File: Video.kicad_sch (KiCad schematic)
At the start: 0 parts

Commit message: motherboard: Added SHIFTER to the schematic and tidied up a pile
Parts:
- added R102: 1k, rhais_rcl:R0603, symbol Device:R_Small
- added U13: 74LS04, symbol 74xx:74LS04
- added U15: 74LS86, symbol 74xx:74LS86
- added U40: GST_SHIFTER, Package_LCC:PLCC-84_SMD-Socket, symbol dragonSTe:GST_SHIFTER
- added U41: 74LS257, symbol 74xx:74LS257
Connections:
- new net: U13.3, U40.21 (SD7)
- new net: R102.1, U40.50 (MONO)
- new net: U41.2 (I0a), U41.6 (I1b)
- new net: U13.5, U15.3
- new net +5V: U40.11 (VDD), U40.32 (VDD), U41.16 (VCC), U41.5 (I0b)
- new net 32MHz: U41.3 (I1a)
- new net DE: U40.54 (DE)
- new net FCLK: U40.34 (FCLK)
- new net GND: U15.10, U15.4, U15.5, U15.9, U40.73 (LOWP), U40.74 (GND), U40.75 (GND), U41.10 (I1d), U41.11 (I0d), U41.13 (I1c), U41.14 (I0c), U41.15 (OE), U41.8 (GND)
- new net MC: U40.53 (CLK), U41.4 (Za)
- new net MICROWIRE_CLK: U40.31 (MWC)
- new net MICROWIRE_DATA: U40.30 (MWD)
- new net MONO_MON: U41.7 (Zb)
- new net SCLK: U40.33 (SCLK)
- new net Sound.D0: U40.28 (SD0)
- new net Sound.D1: U40.27 (SD1)
- new net Sound.D2: U40.26 (SD2)
- new net Sound.D3: U40.25 (SD3)
- new net Sound.D4: U40.24 (SD4)
- new net Sound.D5: U40.23 (SD5)
- new net Sound.D6: U40.22 (SD6)
- new net Sound.D7: U13.4
- new net SysBus.A1: U40.17 (A1)
- new net SysBus.A2: U40.16 (A2)
- new net SysBus.A3: U40.15 (A3)
- new net SysBus.A4: U40.14 (A4)
- new net SysBus.A5: U40.13 (A5)
- new net SysBus.A6: U40.12 (A6)
- new net SysBus.D0: U40.78 (PD0)
- new net SysBus.D1: U40.79 (PD1)
- new net SysBus.D10: U40.4 (PD10)
- new net SysBus.D11: U40.5 (PD11)
- new net SysBus.D12: U40.6 (PD12)
- new net SysBus.D13: U40.7 (PD13)
- new net SysBus.D14: U40.8 (PD14)
- new net SysBus.D15: U40.9 (PD15)
- new net SysBus.D2: U40.80 (PD2)
- new net SysBus.D3: U40.81 (PD3)
- new net SysBus.D4: U40.82 (PD4)
- new net SysBus.D5: U40.83 (PD5)
- new net SysBus.D6: U40.84 (PD6)
- new net SysBus.D7: U40.1 (PD7)
- new net SysBus.D8: U40.2 (PD8)
- new net SysBus.D9: U40.3 (PD9)
- new net SysBus.R/~{W}: U40.10 (R/~{W})
- new net ~{LD}: U40.19 (~{LD})
- new net ~{MICROWIRE_EN}: U40.29 (~{MWE})
- new net ~{RD}: U40.20 (~{RD})
- no-connect marks 0 -> 2

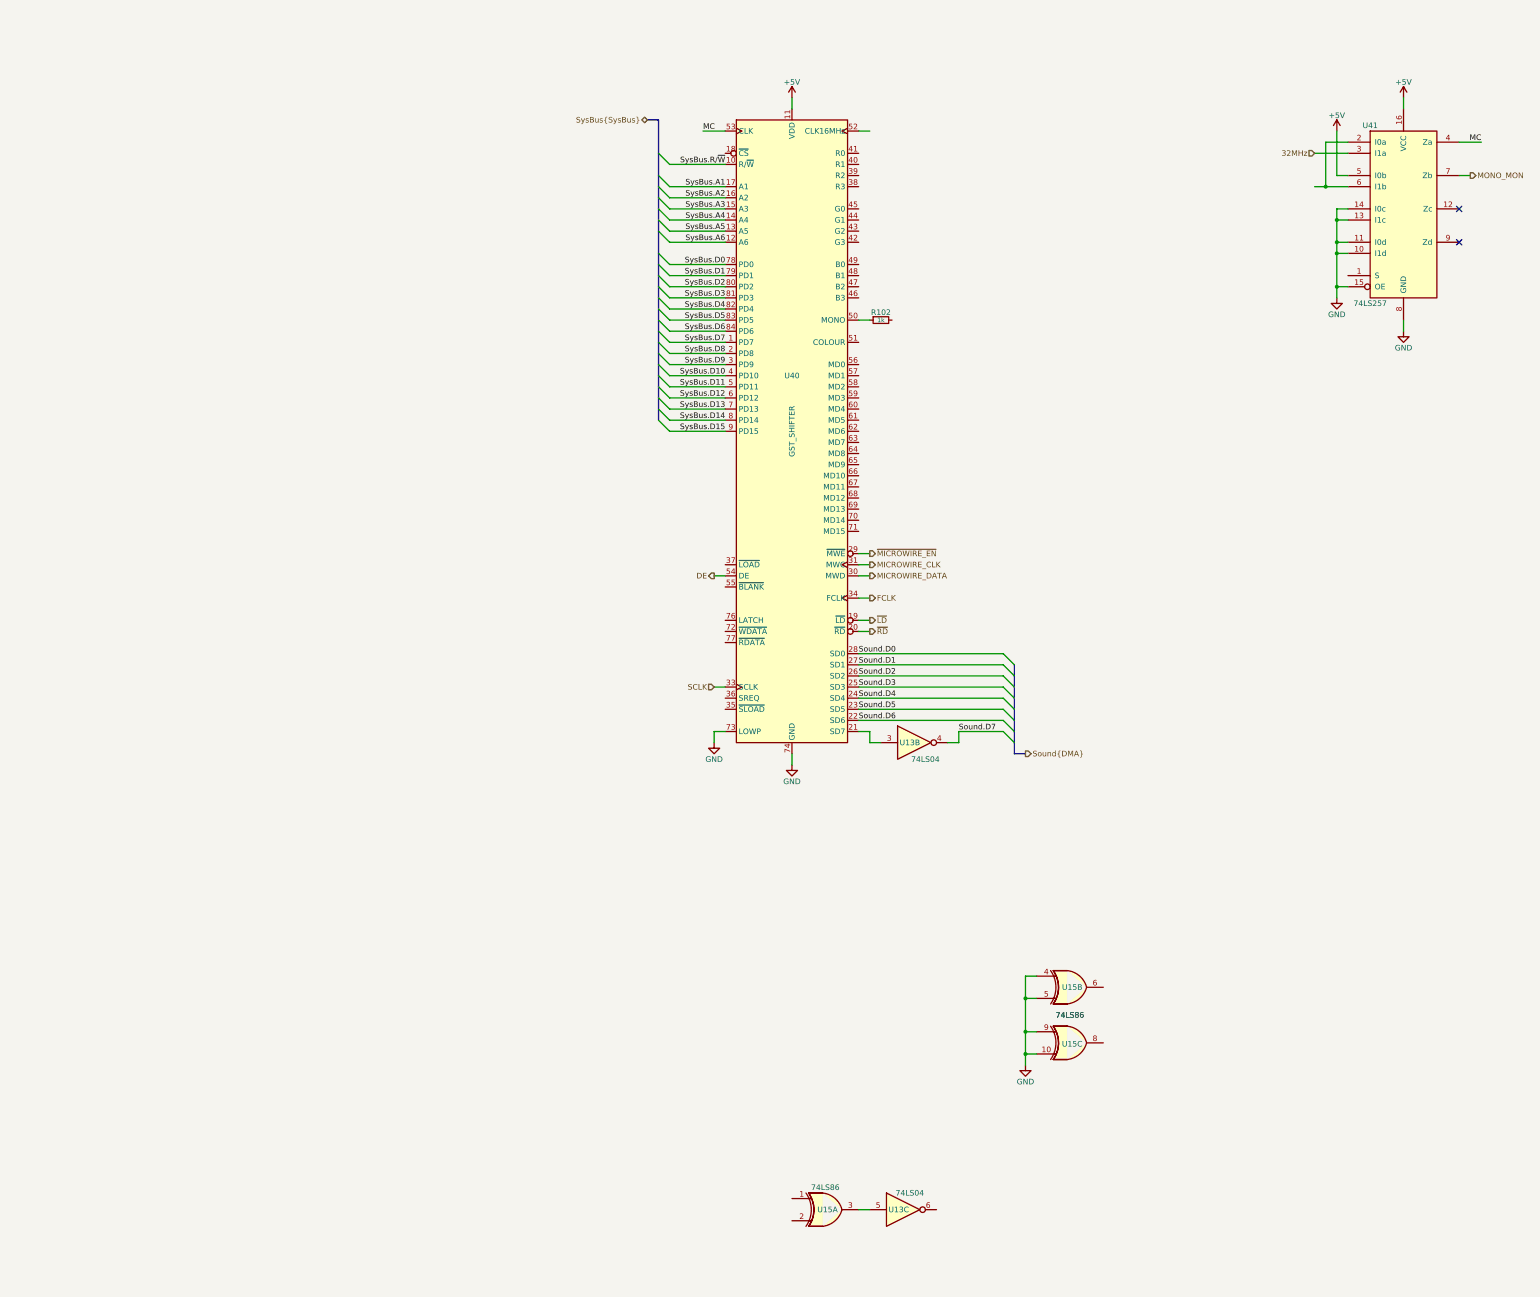
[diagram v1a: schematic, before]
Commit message: motherboard: Further filled out the schematic for the video interface
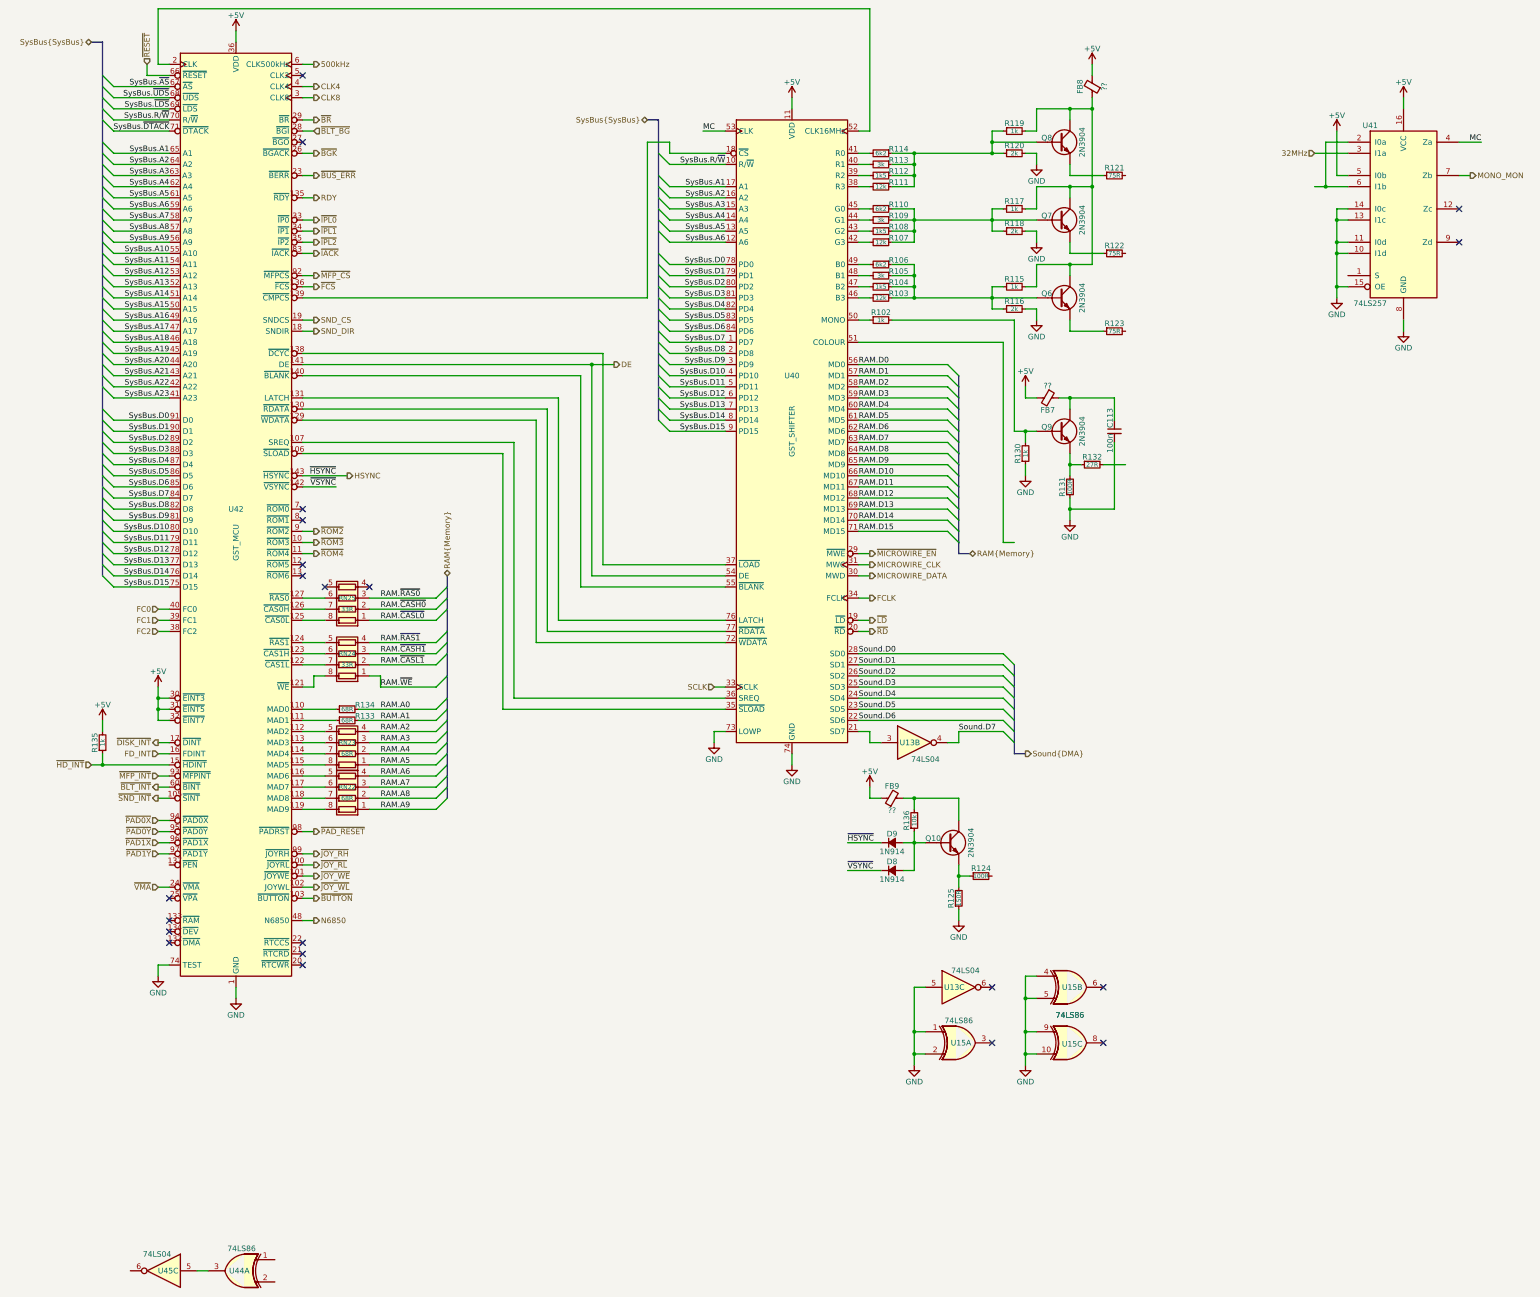
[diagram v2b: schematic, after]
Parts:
- added C113: 100n, rhais_rcl:C0603, symbol Device:C_Small
- added D8, D9: 1N914, symbol Device:D_Small_Filled
- added FB7, FB8, FB9: ??, symbol Device:FerriteBead_Small
- added Q10, Q6, Q7, Q8, Q9: 2N3904, symbol Device:Q_NPN
- added R103, R107, R111: 12k, rhais_rcl:R0603, symbol Device:R_Small
- added R104, R108, R112: 1k5, rhais_rcl:R0603, symbol Device:R_Small
- added R105, R109, R113: 3k, rhais_rcl:R0603, symbol Device:R_Small
- added R106, R110, R114: 6k2, rhais_rcl:R0603, symbol Device:R_Small
- added R115, R117, R119, R130, R135: 1k, rhais_rcl:R0603, symbol Device:R_Small
- added R116, R118, R120: 2k, rhais_rcl:R0603, symbol Device:R_Small
- added R121, R122, R123: 75R, rhais_rcl:R0603, symbol Device:R_Small
- added R124, R131: 100R, rhais_rcl:R0603, symbol Device:R_Small
- added R125: 150R, rhais_rcl:R0603, symbol Device:R_Small
- added R132: 27R, rhais_rcl:R0603, symbol Device:R_Small
- added R133, R134: 68R, rhais_rcl:R0603, symbol Device:R_Small
- added R136: 10k, rhais_rcl:R0603, symbol Device:R_Small
- added RN22, RN23: 68R, rhais_rcl:R0603_Array_Concave_4, symbol Device:R_Pack04
- added RN24, RN25: 33R, rhais_rcl:R0603_Array_Concave_4, symbol Device:R_Pack04
- added U42: GST_MCU, Package_QFP:LQFP-144_20x20mm_P0.5mm, symbol dragonSTe:GST_MCU
- added U44: 74LS86, symbol 74xx:74LS86
- added U45: 74LS04, symbol 74xx:74LS04
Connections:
- net +5V: now also FB7.2, FB8.2, FB9.1, R135.2, U42.108 (VDD), U42.120 (VDD), U42.144 (VDD), U42.30 (~{EINT3}), U42.31 (~{EINT5}), U42.32 (~{EINT7}), U42.36 (VDD), U42.72 (VDD)
- net DE: now also U42.141 (DE)
- net GND: now also U13.5, U15.1, U15.2, C113.2, R116.2, R118.2, R120.2, R125.1, R130.1, R131.1, U42.1 (GND), U42.109 (GND), U42.128 (GND), U42.37 (GND), U42.73 (GND), U42.74 (TEST)
- net SysBus.A1: now also U42.65 (A1)
- net SysBus.A2: now also U42.64 (A2)
- net SysBus.A4: now also U42.62 (A4)
- net SysBus.A5: now also U42.61 (A5)
- net SysBus.A6: now also U42.59 (A6)
- net SysBus.D0: now also U42.91 (D0)
- net SysBus.D1: now also U42.90 (D1)
- net SysBus.D10: now also U42.80 (D10)
- net SysBus.D11: now also U42.79 (D11)
- net SysBus.D12: now also U42.78 (D12)
- net SysBus.D13: now also U42.77 (D13)
- net SysBus.D14: now also U42.76 (D14)
- net SysBus.D15: now also U42.75 (D15)
- net SysBus.D2: now also U42.89 (D2)
- net SysBus.D3: now also U42.88 (D3)
- net SysBus.D4: now also U42.87 (D4)
- net SysBus.D5: now also U42.86 (D5)
- net SysBus.D6: now also U42.85 (D6)
- net SysBus.D7: now also U42.84 (D7)
- net SysBus.D8: now also U42.82 (D8)
- net SysBus.D9: now also U42.81 (D9)
- net SysBus.R/~{W}: now also U42.70 (R/~{W})
- net at U40.18 (~{CS}): now also U42.139 (~{CMPCS})
- net at U40.35 (~{SLOAD}): now also U42.106 (~{SLOAD})
- net at U40.36 (SREQ): now also U42.107 (SREQ)
- net at U40.37 (~{LOAD}): now also U42.138 (~{DCYC})
- net at U40.38 (R3): now also R111.2
- net at U40.39 (R2): now also R112.2
- net at U40.40 (R1): now also R113.2
- net at U40.41 (R0): now also R114.2
- net at U40.42 (G3): now also R107.2
- net at U40.43 (G2): now also R108.2
- net at U40.44 (G1): now also R109.2
- net at U40.45 (G0): now also R110.2
- net at U40.46 (B3): now also R103.2
- net at U40.47 (B2): now also R104.2
- net at U40.48 (B1): now also R105.2
- net at U40.49 (B0): now also R106.2
- net at U40.52 (CLK16MHz): now also U42.2 (CLK)
- net at U40.55 (~{BLANK}): now also U42.140 (~{BLANK})
- net RAM.D0: now reaches U40.56 (MD0)
- net RAM.D1: now reaches U40.57 (MD1)
- net RAM.D2: now reaches U40.58 (MD2)
- net RAM.D3: now reaches U40.59 (MD3)
- net RAM.D4: now reaches U40.60 (MD4)
- net RAM.D5: now reaches U40.61 (MD5)
- net RAM.D6: now reaches U40.62 (MD6)
- net RAM.D7: now reaches U40.63 (MD7)
- net RAM.D8: now reaches U40.64 (MD8)
- net RAM.D9: now reaches U40.65 (MD9)
- net RAM.D10: now reaches U40.66 (MD10)
- net RAM.D11: now reaches U40.67 (MD11)
- net RAM.D12: now reaches U40.68 (MD12)
- net RAM.D13: now reaches U40.69 (MD13)
- net RAM.D14: now reaches U40.70 (MD14)
- net RAM.D15: now reaches U40.71 (MD15)
- net at U40.72 (~{WDATA}): now also U42.129 (~{WDATA})
- net at U40.76 (LATCH): now also U42.131 (LATCH)
- net at U40.77 (~{RDATA}): now also U42.130 (~{RDATA})
- net at R102.2: now also Q9.B, R130.2
- net at U15.3: no longer U13.5
- new net: Q6.B, R103.1, R104.1, R105.1, R106.1, R115.1, R116.1
- new net: R133.1, U42.111 (MAD1)
- new net: Q9.E, R131.2, R132.1
- new net: Q8.B, R111.1, R112.1, R113.1, R114.1, R119.1, R120.1
- new net: U44.3, U45.5
- new net: FB8.1, Q6.C, Q7.C, Q8.C, R115.2, R117.2, R119.2
- new net: Q8.E, R121.1
- new net: Q7.B, R107.1, R108.1, R109.1, R110.1, R117.1, R118.1
- new net: Q10.E, R124.1, R125.2
- new net: D8.2 (A), D9.2 (A), Q10.B, R136.1
- new net: FB9.2, Q10.C, R136.2
- new net: RN25.6 (R3.2), U42.127 (~{RAS0})
- new net: RN25.7 (R2.2), U42.126 (~{CAS0H})
- new net: RN25.8 (R1.2), U42.125 (~{CAS0L})
- new net: Q7.E, R122.1
- new net: Q6.E, R123.1
- new net: C113.1, FB7.1, Q9.C
- new net: R134.1, U42.110 (MAD0)
- new net: RN23.5 (R4.2), U42.112 (MAD2)
- new net: RN23.6 (R3.2), U42.113 (MAD3)
- new net: RN23.7 (R2.2), U42.114 (MAD4)
- new net: RN23.8 (R1.2), U42.115 (MAD5)
- new net: RN22.5 (R4.2), U42.116 (MAD6)
- new net: RN22.6 (R3.2), U42.117 (MAD7)
- new net: RN22.7 (R2.2), U42.118 (MAD8)
- new net: RN22.8 (R1.2), U42.119 (MAD9)
- new net: RN24.8 (R1.2), U42.121 (~{WE})
- new net: RN24.7 (R2.2), U42.122 (~{CAS1L})
- new net: RN24.6 (R3.2), U42.123 (~{CAS1H})
- new net: RN24.5 (R4.2), U42.124 (~{RAS1})
- new net 500kHz: U42.6 (CLK500kHz)
- new net CLK4: U42.4 (CLK4)
- new net CLK8: U42.3 (CLK8)
- new net FC0: U42.40 (FC0)
- new net FC1: U42.39 (FC1)
- new net FC2: U42.38 (FC2)
- new net FD_INT: U42.16 (FDINT)
- new net HSYNC: D9.1 (K), U42.143 (~{HSYNC})
- new net N6850: U42.48 (N6850)
- new net RAM.A0: R134.2
- new net RAM.A1: R133.2
- new net RAM.A2: RN23.4 (R4.1)
- new net RAM.A3: RN23.3 (R3.1)
- new net RAM.A4: RN23.2 (R2.1)
- new net RAM.A5: RN23.1 (R1.1)
- new net RAM.A6: RN22.4 (R4.1)
- new net RAM.A7: RN22.3 (R3.1)
- new net RAM.A8: RN22.2 (R2.1)
- new net RAM.A9: RN22.1 (R1.1)
- new net RAM.~{CASH0}: RN25.2 (R2.1)
- new net RAM.~{CASH1}: RN24.3 (R3.1)
- new net RAM.~{CASL0}: RN25.1 (R1.1)
- new net RAM.~{CASL1}: RN24.2 (R2.1)
- new net RAM.~{RAS0}: RN25.3 (R3.1)
- new net RAM.~{RAS1}: RN24.4 (R4.1)
- new net RAM.~{WE}: RN24.1 (R1.1)
- new net RDY: U42.135 (~{RDY})
- new net SND_CS: U42.19 (SNDCS)
- new net SND_DIR: U42.18 (SNDIR)
- new net SysBus.A10: U42.55 (A10)
- new net SysBus.A11: U42.54 (A11)
- new net SysBus.A12: U42.53 (A12)
- new net SysBus.A13: U42.52 (A13)
- new net SysBus.A14: U42.51 (A14)
- new net SysBus.A15: U42.50 (A15)
- new net SysBus.A16: U42.49 (A16)
- new net SysBus.A17: U42.47 (A17)
- new net SysBus.A18: U42.46 (A18)
- new net SysBus.A19: U42.45 (A19)
- new net SysBus.A20: U42.44 (A20)
- new net SysBus.A21: U42.43 (A21)
- new net SysBus.A22: U42.42 (A22)
- new net SysBus.A23: U42.41 (A23)
- new net SysBus.A7: U42.58 (A7)
- new net SysBus.A8: U42.57 (A8)
- new net SysBus.A9: U42.56 (A9)
- new net SysBus.~{AS}: U42.67 (~{AS})
- new net SysBus.~{DTACK}: U42.71 (~{DTACK})
- new net SysBus.~{LDS}: U42.69 (~{LDS})
- new net SysBus.~{UDS}: U42.68 (~{UDS})
- new net ~{BGK}: U42.26 (~{BGACK})
- new net ~{BLT_BG}: U42.28 (~{BGI})
- new net ~{BLT_INT}: U42.60 (~{BINT})
- new net ~{BR}: U42.29 (~{BR})
- new net ~{BUS_ERR}: U42.23 (~{BERR})
- new net ~{BUTTON}: U42.103 (~{BUTTON})
- new net ~{DISK_INT}: U42.17 (~{DINT})
- new net ~{FCS}: U42.136 (~{FCS})
- new net ~{HD_INT}: R135.1, U42.15 (~{HDINT})
- new net ~{IACK}: U42.83 (~{IACK})
- new net ~{IPL0}: U42.33 (~{IP0})
- new net ~{IPL1}: U42.34 (~{IP1})
- new net ~{IPL2}: U42.35 (~{IP2})
- new net ~{JOY_RH}: U42.99 (~{JOYRH})
- new net ~{JOY_RL}: U42.100 (~{JOYRL})
- new net ~{JOY_WE}: U42.101 (~{JOYWE})
- new net ~{JOY_WL}: U42.102 (JOYWL)
- new net ~{MFP_CS}: U42.92 (~{MFPCS})
- new net ~{MFP_INT}: U42.93 (~{MFPINT})
- new net ~{PAD0X}: U42.94 (~{PAD0X})
- new net ~{PAD0Y}: U42.95 (~{PAD0Y})
- new net ~{PAD1X}: U42.96 (~{PAD1X})
- new net ~{PAD1Y}: U42.97 (~{PAD1Y})
- new net ~{PAD_RESET}: U42.98 (~{PADRST})
- new net ~{RESET}: U42.66 (~{RESET})
- new net ~{ROM2}: U42.9 (~{ROM2})
- new net ~{ROM3}: U42.10 (~{ROM3})
- new net ~{ROM4}: U42.11 (~{ROM4})
- new net ~{SND_INT}: U42.105 (~{SINT})
- new net ~{VMA}: U42.24 (~{VMA})
- new net ~{VSYNC}: D8.1 (K), U42.142 (~{VSYNC})
- no-connect marks 2 -> 21
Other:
- moved on the sheet: U13C, U15A

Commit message: motherboard: More signal routing, and starting in on the BoM
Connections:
- net ~{PEN}: now reaches U42.137 (~{PEN})

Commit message: motherboard: Begun routing the FM synth sound chip
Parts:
- U13, U45: footprint (none) -> rhais_package-smd:SO-14_3.9x8.65mm_P1.27mm; MFR (none) -> Nexperia; MPN (none) -> 74HCT14D,653; OC_FARNELL (none) -> 1201304
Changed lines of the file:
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@@
 			)
 		)
-		(property "Footprint" ""
+		(property "Footprint" "rhais_package-smd:SO-14_3.9x8.65mm_P1.27mm"
 			(at 72.39 318.77 0)
 			(effects
@@
 			)
 		)
-		(property "Datasheet" "http://www.ti.com/lit/gpn/sn74LS04"
+		(property "Datasheet" "https://assets.nexperia.com/documents/data-sheet/74HC_HCT14.pdf"
 			(at 72.39 318.77 0)
 			(effects
@@
 		)
 		(property "Description" "Hex Inverter"
+			(at 72.39 318.77 0)
+			(effects
+				(font
+					(size 1.27 1.27)
+				)
+				(hide yes)
+			)
+		)
+		(property "MFR" "Nexperia"
+			(at 72.39 318.77 0)
+			(effects
+				(font
+					(size 1.27 1.27)
+				)
+				(hide yes)
+			)
+		)
+		(property "MPN" "74HCT14D,653"
+			(at 72.39 318.77 0)
+			(effects
+				(font
+					(size 1.27 1.27)
+				)
+				(hide yes)
+			)
+		)
+		(property "OC_FARNELL" "1201304"
 			(at 72.39 318.77 0)
 			(effects
@@
 			)
 		)
-		(property "Footprint" ""
+		(property "Footprint" "rhais_package-smd:SO-14_3.9x8.65mm_P1.27mm"
 			(at 243.84 198.12 0)
 			(effects
@@
 			)
 		)
-		(property "Datasheet" "http://www.ti.com/lit/gpn/sn74LS04"
+		(property "Datasheet" "https://assets.nexperia.com/documents/data-sheet/74HC_HCT14.pdf"
 			(at 243.84 198.12 0)
 			(effects
@@
 		)
 		(property "Description" "Hex Inverter"
+			(at 243.84 198.12 0)
+			(effects
+				(font
+					(size 1.27 1.27)
+				)
+				(hide yes)
+			)
+		)
+		(property "MFR" "Nexperia"
+			(at 243.84 198.12 0)
+			(effects
+				(font
+					(size 1.27 1.27)
+				)
+				(hide yes)
+			)
+		)
+		(property "MPN" "74HCT14D,653"
+			(at 243.84 198.12 0)
+			(effects
+				(font
+					(size 1.27 1.27)
+				)
+				(hide yes)
+			)
+		)
+		(property "OC_FARNELL" "1201304"
 			(at 243.84 198.12 0)
 			(effects
@@
 			)
 		)
-		(property "Footprint" ""
+		(property "Footprint" "rhais_package-smd:SO-14_3.9x8.65mm_P1.27mm"
 			(at 254 254 0)
 			(effects
@@
 			)
 		)
-		(property "Datasheet" "http://www.ti.com/lit/gpn/sn74LS04"
+		(property "Datasheet" "https://assets.nexperia.com/documents/data-sheet/74HC_HCT14.pdf"
 			(at 254 254 0)
 			(effects
@@
 			(at 254 254 0)
 			(effects
+				(font
+					(size 1.27 1.27)
+				)
+				(hide yes)
+			)
+		)
+		(property "MFR" "Nexperia"
+			(at 254 254 0)
+			(effects
+				(font
+					(size 1.27 1.27)
+				)
+				(hide yes)
+			)
+		)
+		(property "MPN" "74HCT14D,653"
+			(at 254 254 0)
+			(effects
+				(font
+					(size 1.27 1.27)
+				)
+				(hide yes)
+			)
+		)
+		(property "OC_FARNELL" "1201304"
+			(at 254 254 0)
+			(effects

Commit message: motherboard: Routed one of the parallel interfaces and the ROMs
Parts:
- Q10, Q6, Q7, Q8, Q9: footprint (none) -> rhais_package-smd:SOT-23
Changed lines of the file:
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@@
 			)
 		)
-		(property "Footprint" ""
+		(property "Footprint" "rhais_package-smd:SOT-23"
 			(at 281.94 58.42 0)
 			(effects
@@
 			)
 		)
-		(property "Footprint" ""
+		(property "Footprint" "rhais_package-smd:SOT-23"
 			(at 256.54 218.44 0)
 			(effects
@@
 			)
 		)
-		(property "Footprint" ""
+		(property "Footprint" "rhais_package-smd:SOT-23"
 			(at 281.94 76.2 0)
 			(effects
@@
 			)
 		)
-		(property "Footprint" ""
+		(property "Footprint" "rhais_package-smd:SOT-23"
 			(at 281.94 124.46 0)
 			(effects
@@
 			)
 		)
-		(property "Footprint" ""
+		(property "Footprint" "rhais_package-smd:SOT-23"
 			(at 281.94 93.98 0)
 			(effects
